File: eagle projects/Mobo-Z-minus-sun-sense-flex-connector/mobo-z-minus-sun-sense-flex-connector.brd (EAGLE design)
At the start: 24.8 x 186.1 mm, 2 parts, among them X1 5X2_SMD_2.54MM_HEADER, X2 5X2_SMD_2.54MM_HEADER

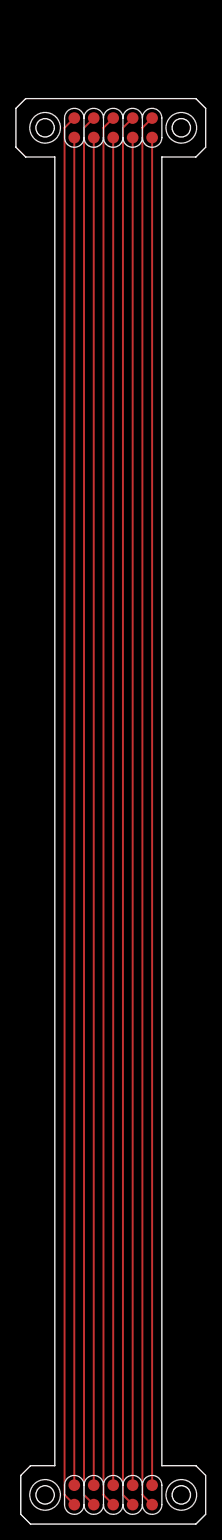
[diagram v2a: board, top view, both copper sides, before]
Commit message: Added 24 pin SMD header and lengthened both connectors
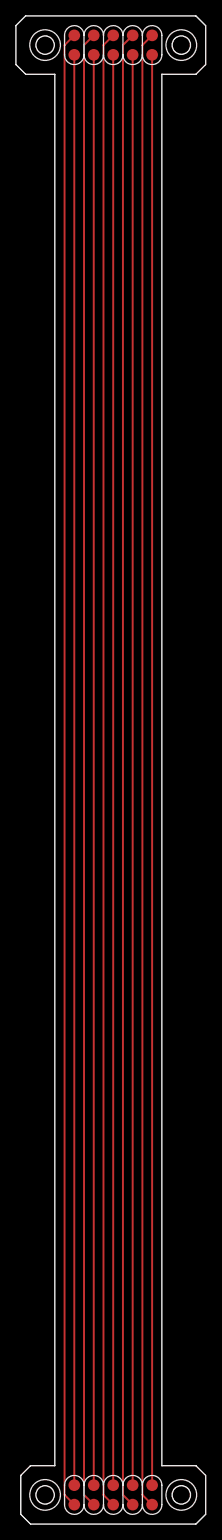
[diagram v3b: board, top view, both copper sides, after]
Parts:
- moved X1 10.8 mm to (10.2, 189.2)
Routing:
- net N$9: track 175.9 -> 186.7 mm
- net N$8: track 175.9 -> 186.7 mm
- net N$6: track 175.9 -> 186.7 mm
- net N$10: track 175.9 -> 186.7 mm
- net N$7: track 176.2 -> 187.0 mm
- net N$5: track 182.0 -> 192.8 mm
- net N$4: track 182.0 -> 192.8 mm
- net N$3: track 182.0 -> 192.8 mm
- net N$2: track 182.0 -> 192.8 mm
- net N$1: track 182.0 -> 192.8 mm
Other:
- board size 24.8 x 186.1 mm -> 24.8 x 196.8 mm
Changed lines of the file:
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@@
 <board>
 <plain>
-<hole x="1.27" y="178.435" drill="2.4"/>
-<circle x="1.27" y="178.435" radius="2" width="0.1524" layer="21"/>
-<hole x="19.05" y="178.435" drill="2.4"/>
-<circle x="19.05" y="178.435" radius="2" width="0.1524" layer="21"/>
+<hole x="1.27" y="189.23" drill="2.4"/>
+<circle x="1.27" y="189.23" radius="2" width="0.1524" layer="21"/>
+<hole x="19.05" y="189.23" drill="2.4"/>
+<circle x="19.05" y="189.23" radius="2" width="0.1524" layer="21"/>
 <hole x="1.27" y="0" drill="2.4"/>
 <circle x="1.27" y="0" radius="2" width="0.1524" layer="21"/>
@@
 <circle x="19.05" y="0" radius="2" width="0.1524" layer="21"/>
 <text x="24.13" y="22.86" size="1.778" layer="48">need atleast 163.93 mm length</text>
-<dimension x1="-4.445" y1="1.905" x2="-4.445" y2="175.895" x3="-19.05" y3="88.9" textsize="1.778" layer="1"/>
+<dimension x1="-4.445" y1="1.905" x2="-4.445" y2="186.69" x3="-19.05" y3="94.2975" textsize="1.778" layer="1"/>
 <wire x1="-1.905" y1="-2.54" x2="-1.905" y2="2.54" width="0.1524" layer="20"/>
 <wire x1="22.225" y1="2.54" x2="22.225" y2="-2.54" width="0.1524" layer="20"/>
-<wire x1="-2.54" y1="175.895" x2="-2.54" y2="180.975" width="0.1524" layer="20"/>
-<wire x1="22.225" y1="175.895" x2="22.225" y2="180.975" width="0.1524" layer="20"/>
-<wire x1="-2.54" y1="180.975" x2="-1.27" y2="182.245" width="0.1524" layer="20"/>
-<wire x1="-1.27" y1="182.245" x2="20.955" y2="182.245" width="0.1524" layer="20"/>
-<wire x1="20.955" y1="182.245" x2="22.225" y2="180.975" width="0.1524" layer="20"/>
-<wire x1="-2.54" y1="175.895" x2="-1.27" y2="174.625" width="0.1524" layer="20"/>
-<wire x1="22.225" y1="175.895" x2="20.955" y2="174.625" width="0.1524" layer="20"/>
+<wire x1="-2.54" y1="186.69" x2="-2.54" y2="191.77" width="0.1524" layer="20"/>
+<wire x1="22.225" y1="186.69" x2="22.225" y2="191.77" width="0.1524" layer="20"/>
+<wire x1="-2.54" y1="191.77" x2="-1.27" y2="193.04" width="0.1524" layer="20"/>
+<wire x1="-1.27" y1="193.04" x2="20.955" y2="193.04" width="0.1524" layer="20"/>
+<wire x1="20.955" y1="193.04" x2="22.225" y2="191.77" width="0.1524" layer="20"/>
+<wire x1="-2.54" y1="186.69" x2="-1.27" y2="185.42" width="0.1524" layer="20"/>
+<wire x1="22.225" y1="186.69" x2="20.955" y2="185.42" width="0.1524" layer="20"/>
 <wire x1="-1.905" y1="2.54" x2="-0.635" y2="3.81" width="0.1524" layer="20"/>
 <wire x1="-1.905" y1="-2.54" x2="-0.635" y2="-3.81" width="0.1524" layer="20"/>
@@
 <wire x1="-0.635" y1="3.81" x2="2.54" y2="3.81" width="0.1524" layer="20"/>
 <wire x1="20.955" y1="3.81" x2="16.51" y2="3.81" width="0.1524" layer="20"/>
-<wire x1="-1.27" y1="174.625" x2="2.54" y2="174.625" width="0.1524" layer="20"/>
-<wire x1="20.955" y1="174.625" x2="16.51" y2="174.625" width="0.1524" layer="20"/>
-<wire x1="2.54" y1="174.625" x2="2.54" y2="3.81" width="0.1524" layer="20"/>
-<wire x1="16.51" y1="3.81" x2="16.51" y2="174.625" width="0.1524" layer="20"/>
+<wire x1="-1.27" y1="185.42" x2="2.54" y2="185.42" width="0.1524" layer="20"/>
+<wire x1="20.955" y1="185.42" x2="16.51" y2="185.42" width="0.1524" layer="20"/>
+<wire x1="2.54" y1="185.42" x2="2.54" y2="3.81" width="0.1524" layer="20"/>
+<wire x1="16.51" y1="3.81" x2="16.51" y2="185.42" width="0.1524" layer="20"/>
 </plain>
 <attributes>
@@
 </autorouter>
 <elements>
-<element name="X1" library="SMD_headers" package="5X2_HEADER" value="5X2_SMD_2.54MM_HEADER" x="10.16" y="178.435" smashed="yes" rot="R180"/>
+<element name="X1" library="SMD_headers" package="5X2_HEADER" value="5X2_SMD_2.54MM_HEADER" x="10.16" y="189.23" smashed="yes" rot="R180"/>
 <element name="X2" library="SMD_headers" package="5X2_HEADER" value="5X2_SMD_2.54MM_HEADER" x="10.16" y="0" smashed="yes"/>
 </elements>
@@
 <contactref element="X1" pad="P1"/>
 <contactref element="X2" pad="P5"/>
-<wire x1="5.08" y1="177.165" x2="5.08" y2="1.27" width="0.254" layer="1"/>
+<wire x1="5.08" y1="187.96" x2="5.08" y2="1.27" width="0.254" layer="1"/>
+<wire x1="5.08" y1="1.27" x2="5.08" y2="187.96" width="0" layer="19"/>
+<wire x1="5.08" y1="1.27" x2="5.08" y2="187.96" width="0" layer="19"/>
+<wire x1="5.08" y1="1.27" x2="5.08" y2="187.96" width="0" layer="19"/>
 </signal>
 <signal name="N$7">
 <contactref element="X1" pad="P2"/>
 <contactref element="X2" pad="P4"/>
-<wire x1="7.62" y1="1.27" x2="7.62" y2="176.53" width="0.254" layer="1"/>
-<wire x1="7.62" y1="176.53" x2="8.255" y2="177.165" width="0.254" layer="1"/>
-<wire x1="8.255" y1="177.165" x2="7.62" y2="177.165" width="0" layer="19" extent="1-1"/>
+<wire x1="7.62" y1="1.27" x2="7.62" y2="187.325" width="0.254" layer="1"/>
+<wire x1="7.62" y1="187.325" x2="8.255" y2="187.96" width="0.254" layer="1"/>
+<wire x1="8.255" y1="187.96" x2="7.62" y2="187.96" width="0" layer="19" extent="1-1"/>
 </signal>
 <signal name="N$8">
 <contactref element="X1" pad="P3"/>
 <contactref element="X2" pad="P3"/>
-<wire x1="10.16" y1="177.165" x2="10.16" y2="1.27" width="0.254" layer="1"/>
+<wire x1="10.16" y1="187.96" x2="10.16" y2="1.27" width="0.254" layer="1"/>
+<wire x1="10.16" y1="1.27" x2="10.16" y2="187.96" width="0" layer="19"/>
+<wire x1="10.16" y1="1.27" x2="10.16" y2="187.96" width="0" layer="19"/>
+<wire x1="10.16" y1="1.27" x2="10.16" y2="187.96" width="0" layer="19"/>
 </signal>
 <signal name="N$9">
 <contactref element="X1" pad="P4"/>
 <contactref element="X2" pad="P2"/>
-<wire x1="12.7" y1="1.27" x2="12.7" y2="177.165" width="0.254" layer="1"/>
+<wire x1="12.7" y1="1.27" x2="12.7" y2="187.96" width="0.254" layer="1"/>
+<wire x1="12.7" y1="1.27" x2="12.7" y2="187.96" width="0" layer="19"/>
+<wire x1="12.7" y1="1.27" x2="12.7" y2="187.96" width="0" layer="19"/>
+<wire x1="12.7" y1="1.27" x2="12.7" y2="187.96" width="0" layer="19"/>
 </signal>
 <signal name="N$10">
 <contactref element="X1" pad="P5"/>
 <contactref element="X2" pad="P1"/>
-<wire x1="15.24" y1="177.165" x2="15.24" y2="1.27" width="0.254" layer="1"/>
+<wire x1="15.24" y1="187.96" x2="15.24" y2="1.27" width="0.254" layer="1"/>
+<wire x1="15.24" y1="187.96" x2="15.24" y2="1.27" width="0" layer="19"/>
+<wire x1="15.24" y1="187.96" x2="15.24" y2="1.27" width="0" layer="19"/>
+<wire x1="15.24" y1="187.96" x2="15.24" y2="1.27" width="0" layer="19"/>
 </signal>
 <signal name="N$1">
@@
 <contactref element="X2" pad="P10"/>
 <wire x1="5.08" y1="-1.27" x2="3.81" y2="0" width="0.254" layer="1"/>
-<wire x1="3.81" y1="0" x2="3.81" y2="178.435" width="0.254" layer="1"/>
-<wire x1="3.81" y1="178.435" x2="5.08" y2="179.705" width="0.254" layer="1"/>
+<wire x1="3.81" y1="0" x2="3.81" y2="189.23" width="0.254" layer="1"/>
+<wire x1="3.81" y1="189.23" x2="5.08" y2="190.5" width="0.254" layer="1"/>
 </signal>
 <signal name="N$2">
 <contactref element="X1" pad="P7"/>
 <contactref element="X2" pad="P9"/>
-<wire x1="7.62" y1="179.705" x2="6.35" y2="178.435" width="0.254" layer="1"/>
-<wire x1="6.35" y1="178.435" x2="6.35" y2="0" width="0.254" layer="1"/>
+<wire x1="7.62" y1="190.5" x2="6.35" y2="189.23" width="0.254" layer="1"/>
+<wire x1="6.35" y1="189.23" x2="6.35" y2="0" width="0.254" layer="1"/>
 <wire x1="6.35" y1="0" x2="7.62" y2="-1.27" width="0.254" layer="1"/>
 </signal>
@@
 <contactref element="X2" pad="P8"/>
 <wire x1="10.16" y1="-1.27" x2="8.89" y2="0" width="0.254" layer="1"/>
-<wire x1="8.89" y1="0" x2="8.89" y2="178.435" width="0.254" layer="1"/>
-<wire x1="8.89" y1="178.435" x2="10.16" y2="179.705" width="0.254" layer="1"/>
+<wire x1="8.89" y1="0" x2="8.89" y2="189.23" width="0.254" layer="1"/>
+<wire x1="8.89" y1="189.23" x2="10.16" y2="190.5" width="0.254" layer="1"/>
 </signal>
 <signal name="N$4">
 <contactref element="X1" pad="P9"/>
 <contactref element="X2" pad="P7"/>
-<wire x1="12.7" y1="179.705" x2="11.43" y2="178.435" width="0.254" layer="1"/>
-<wire x1="11.43" y1="178.435" x2="11.43" y2="0" width="0.254" layer="1"/>
+<wire x1="12.7" y1="190.5" x2="11.43" y2="189.23" width="0.254" layer="1"/>
+<wire x1="11.43" y1="189.23" x2="11.43" y2="0" width="0.254" layer="1"/>
 <wire x1="12.7" y1="-1.27" x2="11.43" y2="0" width="0.254" layer="1"/>
 </signal>
@@
 <contactref element="X2" pad="P6"/>
 <wire x1="15.24" y1="-1.27" x2="13.97" y2="0" width="0.254" layer="1"/>
-<wire x1="13.97" y1="178.435" x2="15.24" y2="179.705" width="0.254" layer="1"/>
-<wire x1="13.97" y1="0" x2="13.97" y2="178.435" width="0.254" layer="1"/>
+<wire x1="13.97" y1="189.23" x2="15.24" y2="190.5" width="0.254" layer="1"/>
+<wire x1="13.97" y1="0" x2="13.97" y2="189.23" width="0.254" layer="1"/>
 </signal>
 </signals>

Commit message: Added stiffener polygons
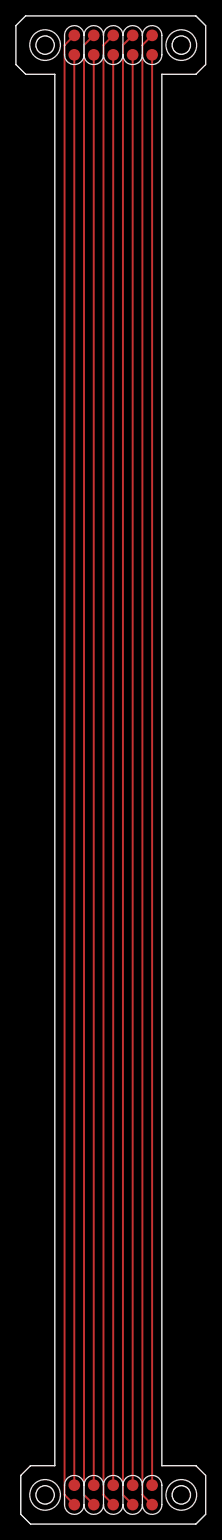
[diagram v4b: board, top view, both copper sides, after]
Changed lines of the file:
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@@
 <layer number="97" name="Info" color="7" fill="1" visible="no" active="no"/>
 <layer number="98" name="Guide" color="6" fill="1" visible="no" active="no"/>
+<layer number="114" name="Stiffener" color="45" fill="1" visible="yes" active="yes"/>
 </layers>
 <board>
@@
 <wire x1="2.54" y1="185.42" x2="2.54" y2="3.81" width="0.1524" layer="20"/>
 <wire x1="16.51" y1="3.81" x2="16.51" y2="185.42" width="0.1524" layer="20"/>
+<polygon width="0.1524" layer="114">
+<vertex x="2.54" y="185.42"/>
+<vertex x="-1.27" y="185.42"/>
+<vertex x="-2.54" y="186.69"/>
+<vertex x="-2.54" y="191.77"/>
+<vertex x="-1.27" y="193.04"/>
+<vertex x="20.955" y="193.04"/>
+<vertex x="22.225" y="191.77"/>
+<vertex x="22.225" y="186.69"/>
+<vertex x="20.955" y="185.42"/>
+</polygon>
+<polygon width="0.1524" layer="114">
+<vertex x="2.54" y="3.81"/>
+<vertex x="-0.635" y="3.81"/>
+<vertex x="-1.905" y="2.54"/>
+<vertex x="-1.905" y="-2.54"/>
+<vertex x="-0.635" y="-3.81"/>
+<vertex x="20.955" y="-3.81"/>
+<vertex x="22.225" y="-2.54"/>
+<vertex x="22.225" y="2.54"/>
+<vertex x="20.955" y="3.81"/>
+</polygon>
 </plain>
 <attributes>
@@
 <contactref element="X1" pad="P1"/>
 <contactref element="X2" pad="P5"/>
-<wire x1="5.08" y1="187.96" x2="5.08" y2="1.27" width="0.254" layer="1"/>
-<wire x1="5.08" y1="1.27" x2="5.08" y2="187.96" width="0" layer="19"/>
-<wire x1="5.08" y1="1.27" x2="5.08" y2="187.96" width="0" layer="19"/>
-<wire x1="5.08" y1="1.27" x2="5.08" y2="187.96" width="0" layer="19"/>
+<wire x1="5.08" y1="1.27" x2="5.08" y2="187.96" width="0.254" layer="1"/>
 </signal>
 <signal name="N$7">
 <contactref element="X1" pad="P2"/>
 <contactref element="X2" pad="P4"/>
-<wire x1="7.62" y1="1.27" x2="7.62" y2="187.325" width="0.254" layer="1"/>
-<wire x1="7.62" y1="187.325" x2="8.255" y2="187.96" width="0.254" layer="1"/>
-<wire x1="8.255" y1="187.96" x2="7.62" y2="187.96" width="0" layer="19" extent="1-1"/>
+<wire x1="7.62" y1="187.96" x2="7.62" y2="1.27" width="0.254" layer="1"/>
 </signal>
 <signal name="N$8">
 <contactref element="X1" pad="P3"/>
 <contactref element="X2" pad="P3"/>
-<wire x1="10.16" y1="187.96" x2="10.16" y2="1.27" width="0.254" layer="1"/>
-<wire x1="10.16" y1="1.27" x2="10.16" y2="187.96" width="0" layer="19"/>
-<wire x1="10.16" y1="1.27" x2="10.16" y2="187.96" width="0" layer="19"/>
-<wire x1="10.16" y1="1.27" x2="10.16" y2="187.96" width="0" layer="19"/>
+<wire x1="10.16" y1="1.27" x2="10.16" y2="187.96" width="0.254" layer="1"/>
 </signal>
 <signal name="N$9">
 <contactref element="X1" pad="P4"/>
 <contactref element="X2" pad="P2"/>
-<wire x1="12.7" y1="1.27" x2="12.7" y2="187.96" width="0.254" layer="1"/>
-<wire x1="12.7" y1="1.27" x2="12.7" y2="187.96" width="0" layer="19"/>
-<wire x1="12.7" y1="1.27" x2="12.7" y2="187.96" width="0" layer="19"/>
-<wire x1="12.7" y1="1.27" x2="12.7" y2="187.96" width="0" layer="19"/>
+<wire x1="12.7" y1="187.96" x2="12.7" y2="1.27" width="0.254" layer="1"/>
 </signal>
 <signal name="N$10">
@@
 <contactref element="X2" pad="P1"/>
 <wire x1="15.24" y1="187.96" x2="15.24" y2="1.27" width="0.254" layer="1"/>
-<wire x1="15.24" y1="187.96" x2="15.24" y2="1.27" width="0" layer="19"/>
-<wire x1="15.24" y1="187.96" x2="15.24" y2="1.27" width="0" layer="19"/>
-<wire x1="15.24" y1="187.96" x2="15.24" y2="1.27" width="0" layer="19"/>
 </signal>
 <signal name="N$1">
 <contactref element="X1" pad="P6"/>
 <contactref element="X2" pad="P10"/>
-<wire x1="5.08" y1="-1.27" x2="3.81" y2="0" width="0.254" layer="1"/>
-<wire x1="3.81" y1="0" x2="3.81" y2="189.23" width="0.254" layer="1"/>
-<wire x1="3.81" y1="189.23" x2="5.08" y2="190.5" width="0.254" layer="1"/>
+<wire x1="3.81" y1="0" x2="5.08" y2="-1.27" width="0.254" layer="1"/>
+<wire x1="5.08" y1="190.5" x2="3.81" y2="189.23" width="0.254" layer="1"/>
+<wire x1="3.81" y1="189.23" x2="3.81" y2="0" width="0.254" layer="1"/>
 </signal>
 <signal name="N$2">
 <contactref element="X1" pad="P7"/>
 <contactref element="X2" pad="P9"/>
-<wire x1="7.62" y1="190.5" x2="6.35" y2="189.23" width="0.254" layer="1"/>
-<wire x1="6.35" y1="189.23" x2="6.35" y2="0" width="0.254" layer="1"/>
-<wire x1="6.35" y1="0" x2="7.62" y2="-1.27" width="0.254" layer="1"/>
+<wire x1="6.35" y1="189.23" x2="7.62" y2="190.5" width="0.254" layer="1"/>
+<wire x1="7.62" y1="-1.27" x2="6.35" y2="0" width="0.254" layer="1"/>
+<wire x1="6.35" y1="0" x2="6.35" y2="189.23" width="0.254" layer="1"/>
 </signal>
 <signal name="N$3">
 <contactref element="X1" pad="P8"/>
 <contactref element="X2" pad="P8"/>
-<wire x1="10.16" y1="-1.27" x2="8.89" y2="0" width="0.254" layer="1"/>
-<wire x1="8.89" y1="0" x2="8.89" y2="189.23" width="0.254" layer="1"/>
-<wire x1="8.89" y1="189.23" x2="10.16" y2="190.5" width="0.254" layer="1"/>
+<wire x1="8.89" y1="0" x2="10.16" y2="-1.27" width="0.254" layer="1"/>
+<wire x1="10.16" y1="190.5" x2="8.89" y2="189.23" width="0.254" layer="1"/>
+<wire x1="8.89" y1="189.23" x2="8.89" y2="0" width="0.254" layer="1"/>
 </signal>
 <signal name="N$4">
 <contactref element="X1" pad="P9"/>
 <contactref element="X2" pad="P7"/>
-<wire x1="12.7" y1="190.5" x2="11.43" y2="189.23" width="0.254" layer="1"/>
-<wire x1="11.43" y1="189.23" x2="11.43" y2="0" width="0.254" layer="1"/>
+<wire x1="11.43" y1="189.23" x2="12.7" y2="190.5" width="0.254" layer="1"/>
 <wire x1="12.7" y1="-1.27" x2="11.43" y2="0" width="0.254" layer="1"/>
+<wire x1="11.43" y1="0" x2="11.43" y2="189.23" width="0.254" layer="1"/>
 </signal>
 <signal name="N$5">
 <contactref element="X1" pad="P10"/>
 <contactref element="X2" pad="P6"/>
-<wire x1="15.24" y1="-1.27" x2="13.97" y2="0" width="0.254" layer="1"/>
-<wire x1="13.97" y1="189.23" x2="15.24" y2="190.5" width="0.254" layer="1"/>
-<wire x1="13.97" y1="0" x2="13.97" y2="189.23" width="0.254" layer="1"/>
+<wire x1="13.97" y1="0" x2="15.24" y2="-1.27" width="0.254" layer="1"/>
+<wire x1="15.24" y1="190.5" x2="13.97" y2="189.23" width="0.254" layer="1"/>
+<wire x1="13.97" y1="189.23" x2="13.97" y2="0" width="0.254" layer="1"/>
 </signal>
 </signals>
